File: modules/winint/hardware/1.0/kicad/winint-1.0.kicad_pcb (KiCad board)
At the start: 2 copper layers, 75 x 75 mm, 60 parts, among them J1 Screw_Terminal_01x09, J2 Screw_Terminal_01x09, J3 M12-5PIN, J4 RELAYS, K1 SANYOU_SRD_Form_C, K2 SANYOU_SRD_Form_C, Q1 2N2219, Q2 2N2219, SW1 INSTANCE, U1 ROT, U2 DOK, U3 STP, U4 DEP, U5 RET, U6 OVL, U7 Teensy_3.2, U8 TEC2-2411WI, U9 MCP2551-I-P

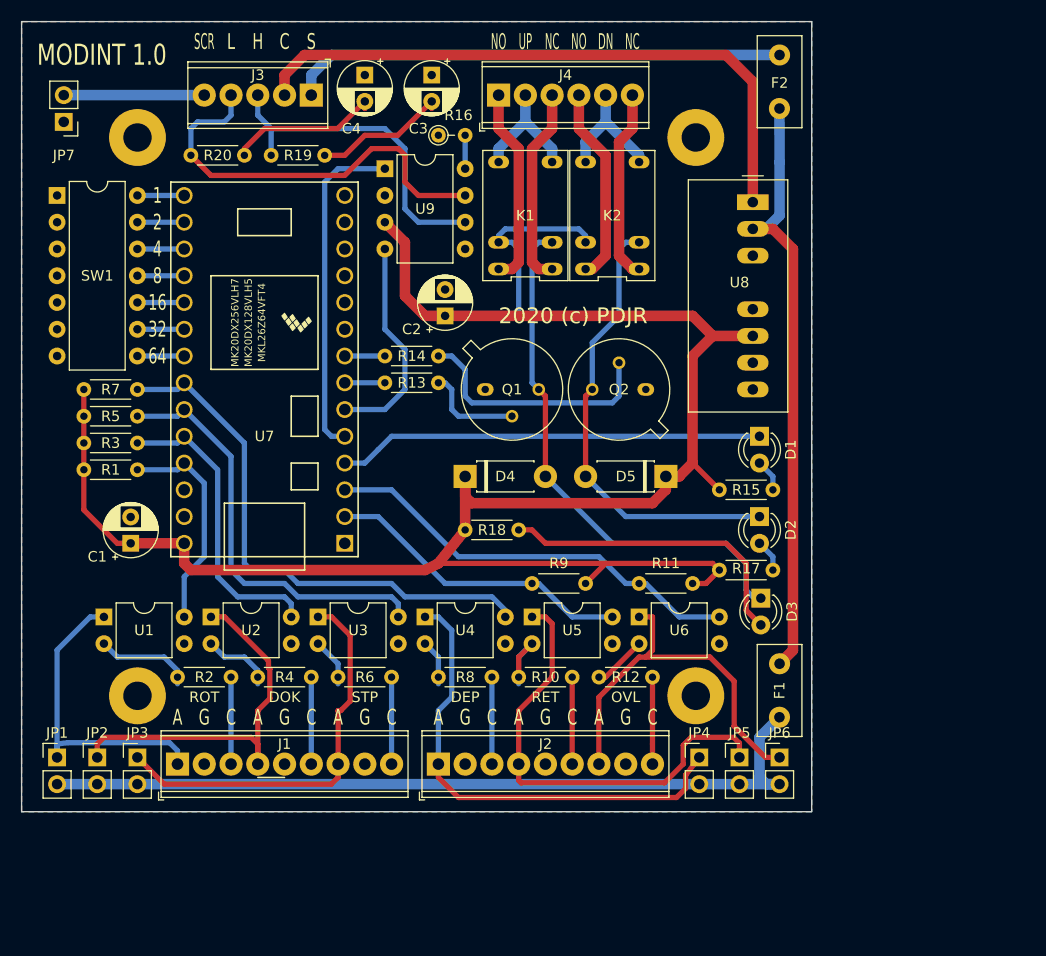
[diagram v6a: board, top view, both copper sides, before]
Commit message: Diode protection on sensor supply
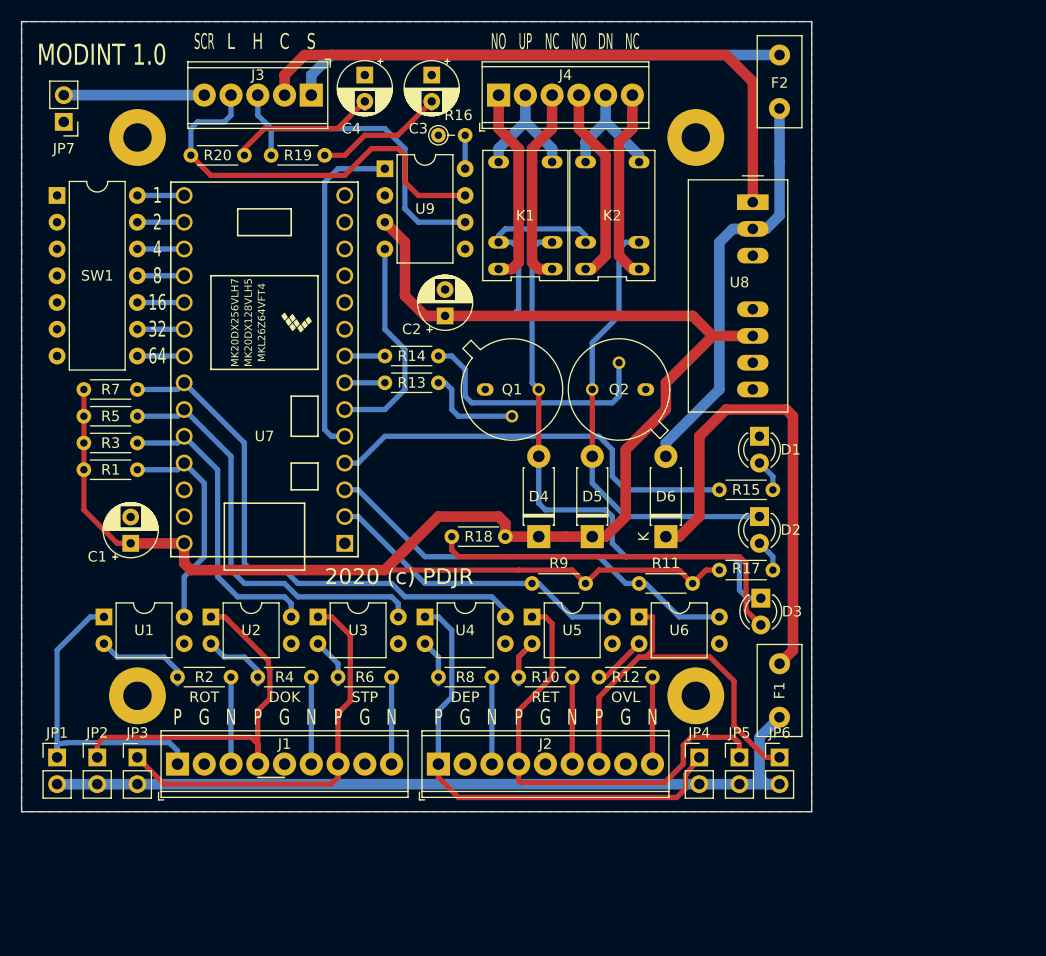
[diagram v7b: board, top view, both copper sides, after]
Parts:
- added D6: 1N4007, Diode_THT:D_DO-41_SOD81_P7.62mm_Horizontal, F.Cu at (197.2, 135.9)
- moved D4 9.03 mm to (185.1, 135.9), turned to 90 degrees
- moved D5 9.03 mm to (190.2, 135.9), turned to 90 degrees
- moved R18 6.38 mm to (176.8, 135.9), turned to 0 degrees
- moved R15 5.08 mm to (202.2, 131.4), turned to 0 degrees
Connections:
- D1 pad 1: Net-(D1-Pad1) -> GND
- F1 pad 1: Net-(F1-Pad1) -> Net-(D6-Pad1)
- F2 pad 2: Net-(F1-Pad1) -> Net-(D6-Pad2)
- R15 pad 1: Net-(D1-Pad2) -> Net-(R15-Pad1)
- R15 pad 2: Net-(C1-Pad1) -> Net-(D1-Pad2)
- U7 pad 4: Net-(D1-Pad1) -> Net-(R15-Pad1)
- U8 pad 2: Net-(F1-Pad1) -> Net-(D6-Pad2)
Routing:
- net Net-(F1-Pad1): track 57.7 -> 0.00 mm
- net Net-(D6-Pad1): track 0.00 -> 45.8 mm
- net Net-(D1-Pad1): track 40.4 -> 0.00 mm
- net Net-(R15-Pad1): track 0.00 -> 40.2 mm
- net Net-(D6-Pad2): track 0.00 -> 39.4 mm
- net Net-(C1-Pad1): track 200.6 -> 192.7 mm
- net Net-(D3-Pad2): track 29.3 -> 36.2 mm
- net Net-(D3-Pad1): track 51.0 -> 54.4 mm
- net Net-(D2-Pad1): track 43.2 -> 42.6 mm
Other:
- board text added: "N"
- board text added: "P"
- board text removed: "A"

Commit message: README edit
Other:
- board text added: "DOWN"
- board text added: "NMEA 2000 Windlass Interface Module"
- board text added: "PWR/RX"
- board text added: "WINT"
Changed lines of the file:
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@@
   (general
     (thickness 1.6)
-    (drawings 65)
+    (drawings 109)
     (tracks 366)
     (zones 0)
@@
   )
   (layers
-    (0 F.Cu signal)
+    (0 F.Cu signal hide)
     (31 B.Cu signal hide)
     (33 F.Adhes user hide)
@@
     (40 Dwgs.User user hide)
     (41 Cmts.User user hide)
-    (42 Eco1.User user hide)
+    (42 Eco1.User user)
     (43 Eco2.User user hide)
     (44 Edge.Cuts user)
@@
     )
   )
+  (gr_line (start 126.71 102.39) (end 126.71 97.39) (layer Eco1.User) (width 0.5))
+  (gr_line (start 132.71 95.39) (end 132.71 104.39) (layer Eco1.User) (width 0.5))
+  (gr_circle (center 200.21 151.23) (end 206.21 151.23) (layer Eco2.User) (width 0.5))
+  (gr_text DOWN (at 205.105 140.335) (layer Eco2.User)
+    (effects (font (size 2 1.5) (thickness 0.375) italic) (justify right))
+  )
+  (gr_text UP (at 205.105 133.985) (layer Eco2.User)
+    (effects (font (size 2 1.5) (thickness 0.375) italic) (justify right))
+  )
+  (gr_line (start 220.71 152.39) (end 220.71 147.39) (layer Eco1.User) (width 0.5))
+  (gr_line (start 216.71 152.39) (end 216.71 147.39) (layer Eco1.User) (width 0.5))
+  (gr_arc (start 218.71 147.39) (end 220.71 147.39) (angle -180) (layer Eco1.User) (width 0.5))
+  (gr_arc (start 218.71 152.39) (end 216.71 152.39) (angle -180) (layer Eco1.User) (width 0.5))
+  (gr_arc (start 218.71 97.39) (end 220.71 97.39) (angle -180) (layer Eco1.User) (width 0.5))
+  (gr_line (start 220.71 102.39) (end 220.71 97.39) (layer Eco1.User) (width 0.5))
+  (gr_arc (start 218.71 102.39) (end 216.71 102.39) (angle -180) (layer Eco1.User) (width 0.5))
+  (gr_line (start 216.71 102.39) (end 216.71 97.39) (layer Eco1.User) (width 0.5))
+  (gr_text WINT (at 138.43 93.98) (layer Eco2.User)
+    (effects (font (size 5 3) (thickness 0.5)) (justify left))
+  )
+  (gr_line (start 132.71 154.39) (end 133.71 154.39) (layer Eco1.User) (width 0.5))
+  (gr_line (start 132.71 145.39) (end 132.71 154.39) (layer Eco1.User) (width 0.5))
+  (gr_line (start 133.71 145.39) (end 132.71 145.39) (layer Eco1.User) (width 0.5))
+  (gr_line (start 132.71 104.39) (end 133.71 104.39) (layer Eco1.User) (width 0.5))
+  (gr_line (start 133.71 95.39) (end 132.71 95.39) (layer Eco1.User) (width 0.5))
+  (gr_circle (center 201.71 152.73) (end 202.21 152.73) (layer Eco2.User) (width 0.5))
+  (gr_circle (center 198.71 152.73) (end 199.21 152.73) (layer Eco2.User) (width 0.5))
+  (gr_circle (center 201.71 149.73) (end 202.21 149.73) (layer Eco2.User) (width 0.5))
+  (gr_circle (center 198.71 149.73) (end 199.21 149.73) (layer Eco2.User) (width 0.5))
+  (gr_circle (center 200.21 151.23) (end 204.71 151.23) (layer Eco2.User) (width 0.5))
+  (gr_circle (center 200.21 151.23) (end 203.745534 151.23) (layer Eco2.User) (width 0.5))
+  (gr_circle (center 200.21 151.23) (end 205.71 151.23) (layer Eco2.User) (width 0.5))
+  (gr_arc (start 218.71 102.39) (end 216.71 102.39) (angle -180) (layer Eco1.User) (width 0.5))
+  (gr_line (start 220.71 102.39) (end 220.71 97.39) (layer Eco1.User) (width 0.5))
+  (gr_arc (start 218.71 97.39) (end 220.71 97.39) (angle -180) (layer Eco1.User) (width 0.5))
+  (gr_line (start 216.71 102.39) (end 216.71 97.39) (layer Eco1.User) (width 0.5))
+  (gr_arc (start 128.71 102.39) (end 126.71 102.39) (angle -180) (layer Eco1.User) (width 0.5))
+  (gr_line (start 130.71 102.39) (end 130.71 97.39) (layer Eco1.User) (width 0.5))
+  (gr_arc (start 128.71 97.39) (end 130.71 97.39) (angle -180) (layer Eco1.User) (width 0.5))
+  (gr_line (start 216.71 152.39) (end 216.71 147.39) (layer Eco1.User) (width 0.5))
+  (gr_arc (start 218.71 152.39) (end 216.71 152.39) (angle -180) (layer Eco1.User) (width 0.5))
+  (gr_line (start 220.71 152.39) (end 220.71 147.39) (layer Eco1.User) (width 0.5))
+  (gr_arc (start 218.71 147.39) (end 220.71 147.39) (angle -180) (layer Eco1.User) (width 0.5))
+  (gr_arc (start 128.71 152.39) (end 126.71 152.39) (angle -180) (layer Eco1.User) (width 0.5))
+  (gr_arc (start 128.71 147.39) (end 130.71 147.39) (angle -180) (layer Eco1.User) (width 0.5))
+  (gr_line (start 126.71 152.39) (end 126.71 147.39) (layer Eco1.User) (width 0.5))
+  (gr_line (start 130.71 152.39) (end 130.71 147.39) (layer Eco1.User) (width 0.5))
+  (gr_line (start 123.71 159.89) (end 133.71 164.89) (layer Eco1.User) (width 0.5))
+  (gr_line (start 123.71 89.89) (end 123.71 159.89) (layer Eco1.User) (width 0.5))
+  (gr_line (start 133.71 84.89) (end 123.71 89.89) (layer Eco1.User) (width 0.5))
+  (gr_line (start 223.71 159.89) (end 213.71 164.89) (layer Eco1.User) (width 0.5))
+  (gr_line (start 223.71 89.89) (end 223.71 159.89) (layer Eco1.User) (width 0.5))
+  (gr_line (start 213.71 84.89) (end 223.71 89.89) (layer Eco1.User) (width 0.5))
+  (gr_text "NMEA 2000 Windlass Interface Module" (at 138.43 99.695) (layer Eco2.User)
+    (effects (font (size 2 1.5) (thickness 0.375) italic) (justify left))
+  )
+  (gr_text PWR/RX (at 205.105 127.635) (layer Eco2.User)
+    (effects (font (size 2 1.5) (thickness 0.375) italic) (justify right))
+  )
+  (gr_circle (center 208.28 140.335) (end 209.699903 140.335) (layer Eco2.User) (width 0.5))
+  (gr_circle (center 208.28 133.985) (end 209.699903 133.985) (layer Eco2.User) (width 0.5))
+  (gr_circle (center 208.28 127.635) (end 209.699903 127.635) (layer Eco2.User) (width 0.5))
+  (gr_line (start 213.71 164.89) (end 133.71 164.89) (layer Eco1.User) (width 0.5))
+  (gr_line (start 213.71 84.89) (end 213.71 164.89) (layer Eco1.User) (width 0.5))
+  (gr_line (start 133.71 84.89) (end 213.71 84.89) (layer Eco1.User) (width 0.5))
+  (gr_line (start 133.71 164.89) (end 133.71 84.89) (layer Eco1.User) (width 0.5))
   (gr_text NC (at 193.98 88.9) (layer F.SilkS)
     (effects (font (size 1.5 0.7) (thickness 0.175)))
@@
     (effects (font (size 1.5 0.7) (thickness 0.175)))
   )
-  (gr_circle (center 200 98) (end 203.81 98) (layer Eco1.User) (width 0.15))
-  (gr_line (start 196.19 97.365) (end 203.81 97.365) (layer Eco1.User) (width 0.15))
-  (gr_line (start 196.19 98.635) (end 203.81 98.635) (layer Eco1.User) (width 0.15))
-  (gr_circle (center 147 98) (end 150.81 98) (layer Eco1.User) (width 0.15))
-  (gr_line (start 143.19 97.365) (end 150.81 97.365) (layer Eco1.User) (width 0.15))
-  (gr_line (start 143.19 98.635) (end 150.81 98.635) (layer Eco1.User) (width 0.15))
-  (gr_circle (center 147 151) (end 150.81 151) (layer Eco1.User) (width 0.15))
-  (gr_line (start 143.19 150.365) (end 150.81 150.365) (layer Eco1.User) (width 0.15))
-  (gr_line (start 143.19 151.635) (end 150.81 151.635) (layer Eco1.User) (width 0.15))
-  (gr_circle (center 200 151) (end 203.81 151) (layer Eco1.User) (width 0.15))
-  (gr_line (start 196.19 150.365) (end 203.81 150.365) (layer Eco1.User) (width 0.15))
-  (gr_line (start 196.19 151.635) (end 203.81 151.635) (layer Eco1.User) (width 0.15))
   (gr_line (start 158.42 158.75) (end 160.96 158.75) (layer F.SilkS) (width 0.15))
   (gr_line (start 123.5 161.5) (end 133.5 164.5) (layer Cmts.User) (width 0.15))
@@
   (segment (start 175.565 149.86) (end 175.565 147.32) (width 0.5) (layer B.Cu) (net 35) (status 10))
   (segment (start 146.99 118.745) (end 151.435 118.745) (width 0.5) (layer B.Cu) (net 36) (status 30))
-  (segment (start 207.95 100.34) (end 207.94 95.25) (width 1) (layer B.Cu) (net 60) (status 20))
-  (segment (start 207.95 105.41) (end 207.95 100.34) (width 1) (layer B.Cu) (net 60))
-  (segment (start 205.41 106.69) (end 206.67 106.69) (width 1) (layer B.Cu) (net 60) (status 30))
-  (segment (start 206.67 106.69) (end 207.95 105.41) (width 1) (layer B.Cu) (net 60) (status 10))
   (segment (start 142.515 143.51) (end 143.815 143.51) (width 0.5) (layer B.Cu) (net 37))
   (segment (start 139.37 146.655) (end 142.515 143.51) (width 0.5) (layer B.Cu) (net 37))
@@
   (segment (start 207.315 130.175) (end 206.045 128.905) (width 0.5) (layer B.Cu) (net 59))
   (segment (start 207.315 131.445) (end 207.315 130.175) (width 0.5) (layer B.Cu) (net 59))
+  (segment (start 207.95 100.34) (end 207.94 95.25) (width 1) (layer B.Cu) (net 60) (status 20))
+  (segment (start 207.95 105.41) (end 207.95 100.34) (width 1) (layer B.Cu) (net 60))
+  (segment (start 205.41 106.69) (end 206.67 106.69) (width 1) (layer B.Cu) (net 60) (status 30))
+  (segment (start 206.67 106.69) (end 207.95 105.41) (width 1) (layer B.Cu) (net 60) (status 10))
   (segment (start 197.155 128.27) (end 197.155 127) (width 1) (layer B.Cu) (net 60))
   (segment (start 197.155 127) (end 202.235 121.92) (width 1) (layer B.Cu) (net 60))
